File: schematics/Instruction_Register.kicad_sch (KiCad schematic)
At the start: 19 parts, among them U1 74LS173, U2 74LS173

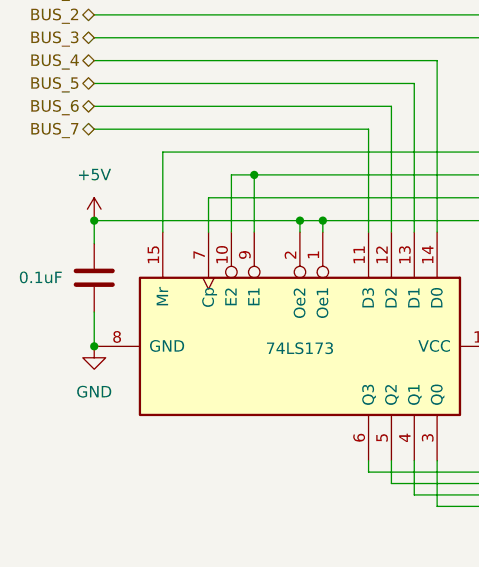
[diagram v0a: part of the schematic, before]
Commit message: feat: updated electrical diagrams & individual part list
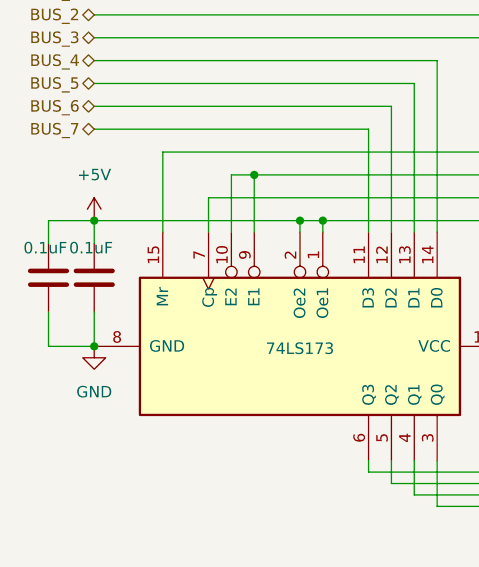
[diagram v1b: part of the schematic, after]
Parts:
- added C2: 0.1uF, symbol Device:C
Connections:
- net +5V: now also C2.1
- net GND: now also C2.2
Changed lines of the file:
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@@
+	(wire
+		(pts
+			(xy 102.87 95.25) (xy 102.87 99.06)
+		)
+		(stroke
+			(width 0)
+			(type default)
+		)
+	)
 	(wire
 		(pts
@@
 	(wire
 		(pts
+			(xy 102.87 85.09) (xy 107.95 85.09)
+		)
+		(stroke
+			(width 0)
+			(type default)
+		)
+	)
+	(wire
+		(pts
 			(xy 160.02 153.67) (xy 163.83 153.67)
 		)
@@
 	(wire
 		(pts
+			(xy 102.87 99.06) (xy 107.95 99.06)
+		)
+		(stroke
+			(width 0)
+			(type default)
+		)
+	)
+	(wire
+		(pts
 			(xy 140.97 72.39) (xy 140.97 86.36)
 		)
@@
 		(pts
 			(xy 107.95 69.85) (xy 143.51 69.85)
+		)
+		(stroke
+			(width 0)
+			(type default)
+		)
+	)
+	(wire
+		(pts
+			(xy 102.87 87.63) (xy 102.87 85.09)
 		)
 		(stroke
@@
 		)
 		(property "Value" "0.1uF"
-			(at 99.568 91.44 0)
+			(at 105.156 88.138 0)
 			(effects
 				(font
@@
 					(unit 1)
 				)
+			)
+		)
+	)
+	(symbol
+		(lib_id "Device:C")
+		(at 102.87 91.44 0)
+		(unit 1)
+		(exclude_from_sim no)
+		(in_bom yes)
+		(on_board yes)
+		(dnp no)
+		(property "Reference" "C2"
+			(at 106.68 90.1699 0)
+			(effects
+				(font
+					(size 1.27 1.27)
+				)
+				(justify left)
+				(hide yes)
+			)
+		)
+		(property "Value" "0.1uF"
+			(at 100.076 88.138 0)
+			(effects
+				(font
+					(size 1.27 1.27)
+				)
+				(justify left)
+			)
+		)
+		(property "Footprint" ""
+			(at 103.8352 95.25 0)
+			(effects
+				(font
+					(size 1.27 1.27)
+				)
+				(hide yes)
+			)
+		)
+		(property "Datasheet" "~"
+			(at 102.87 91.44 0)
+			(effects
+				(font
+					(size 1.27 1.27)
+				)
+				(hide yes)
+			)
+		)
+		(property "Description" "Unpolarized capacitor"
+			(at 102.87 91.44 0)
+			(effects
+				(font
+					(size 1.27 1.27)
+				)
+				(hide yes)
+			)
+		)
+		(pin "2"
+		)
+		(pin "1"
+		)
+		(instances
+			(project "Instruction_Register"
+				(path "/00881835-431f-440c-8b02-f05a8dfd3447"
+					(reference "C2")
+					(unit 1)
+				)
